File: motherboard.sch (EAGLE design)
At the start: 187 parts, among them IC1 LM2576, IC10 TUSB2046B, IC12 LM50, IC13 LM50, IC2 74LS595D, IC3 74LS595D, IC4 IC_FT230X-SSOP-16, IC5 VN5772AK, IC6 VN5772AK, IC7 VN5772AK, IC8 VN5772AK, IC9 VN5772AK, SW1 FSMSM, U2 NCP4625, U3 ATMEGA168, Y1 16Mhz, Y2 6MHz

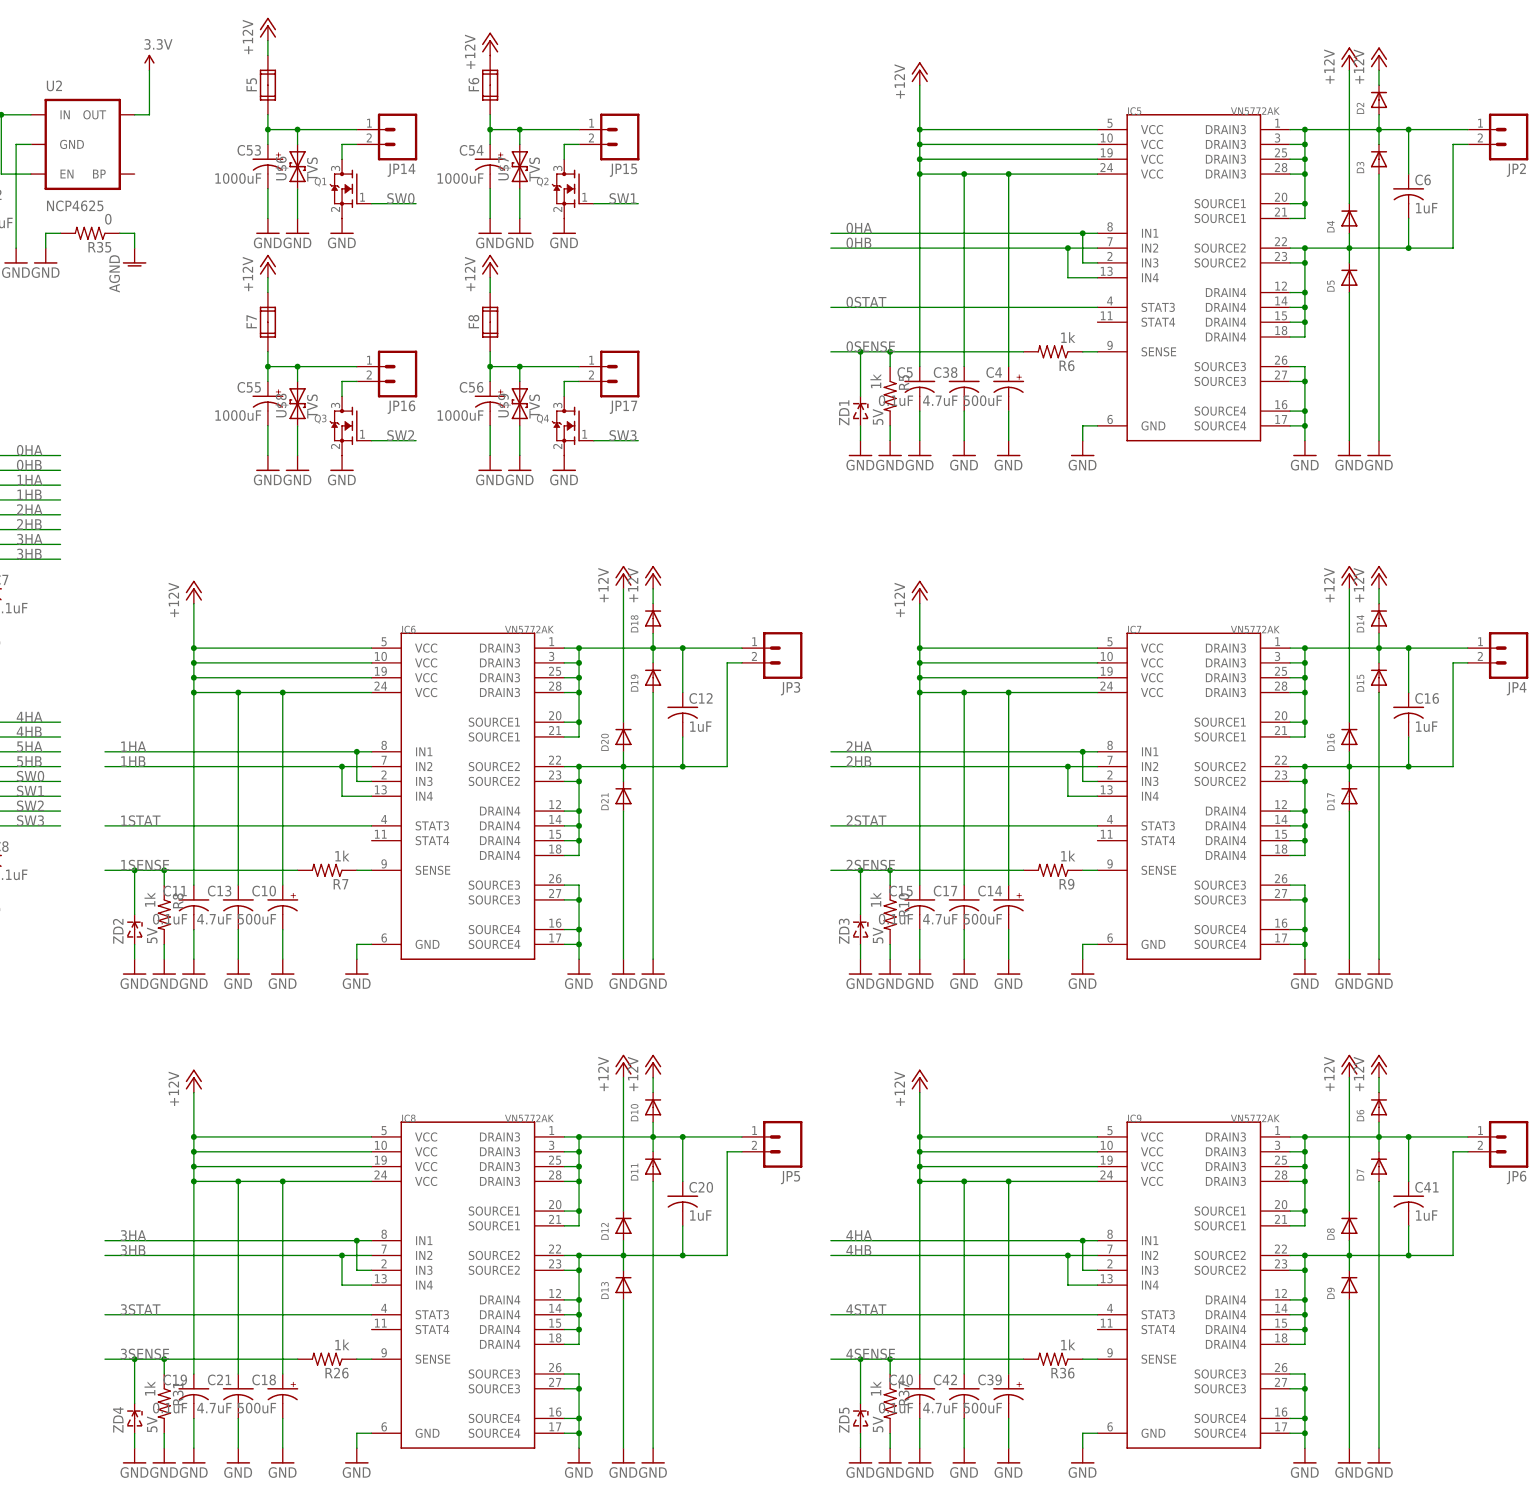
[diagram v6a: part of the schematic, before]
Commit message: rewired h-bridges to not short out and simplified trace layout
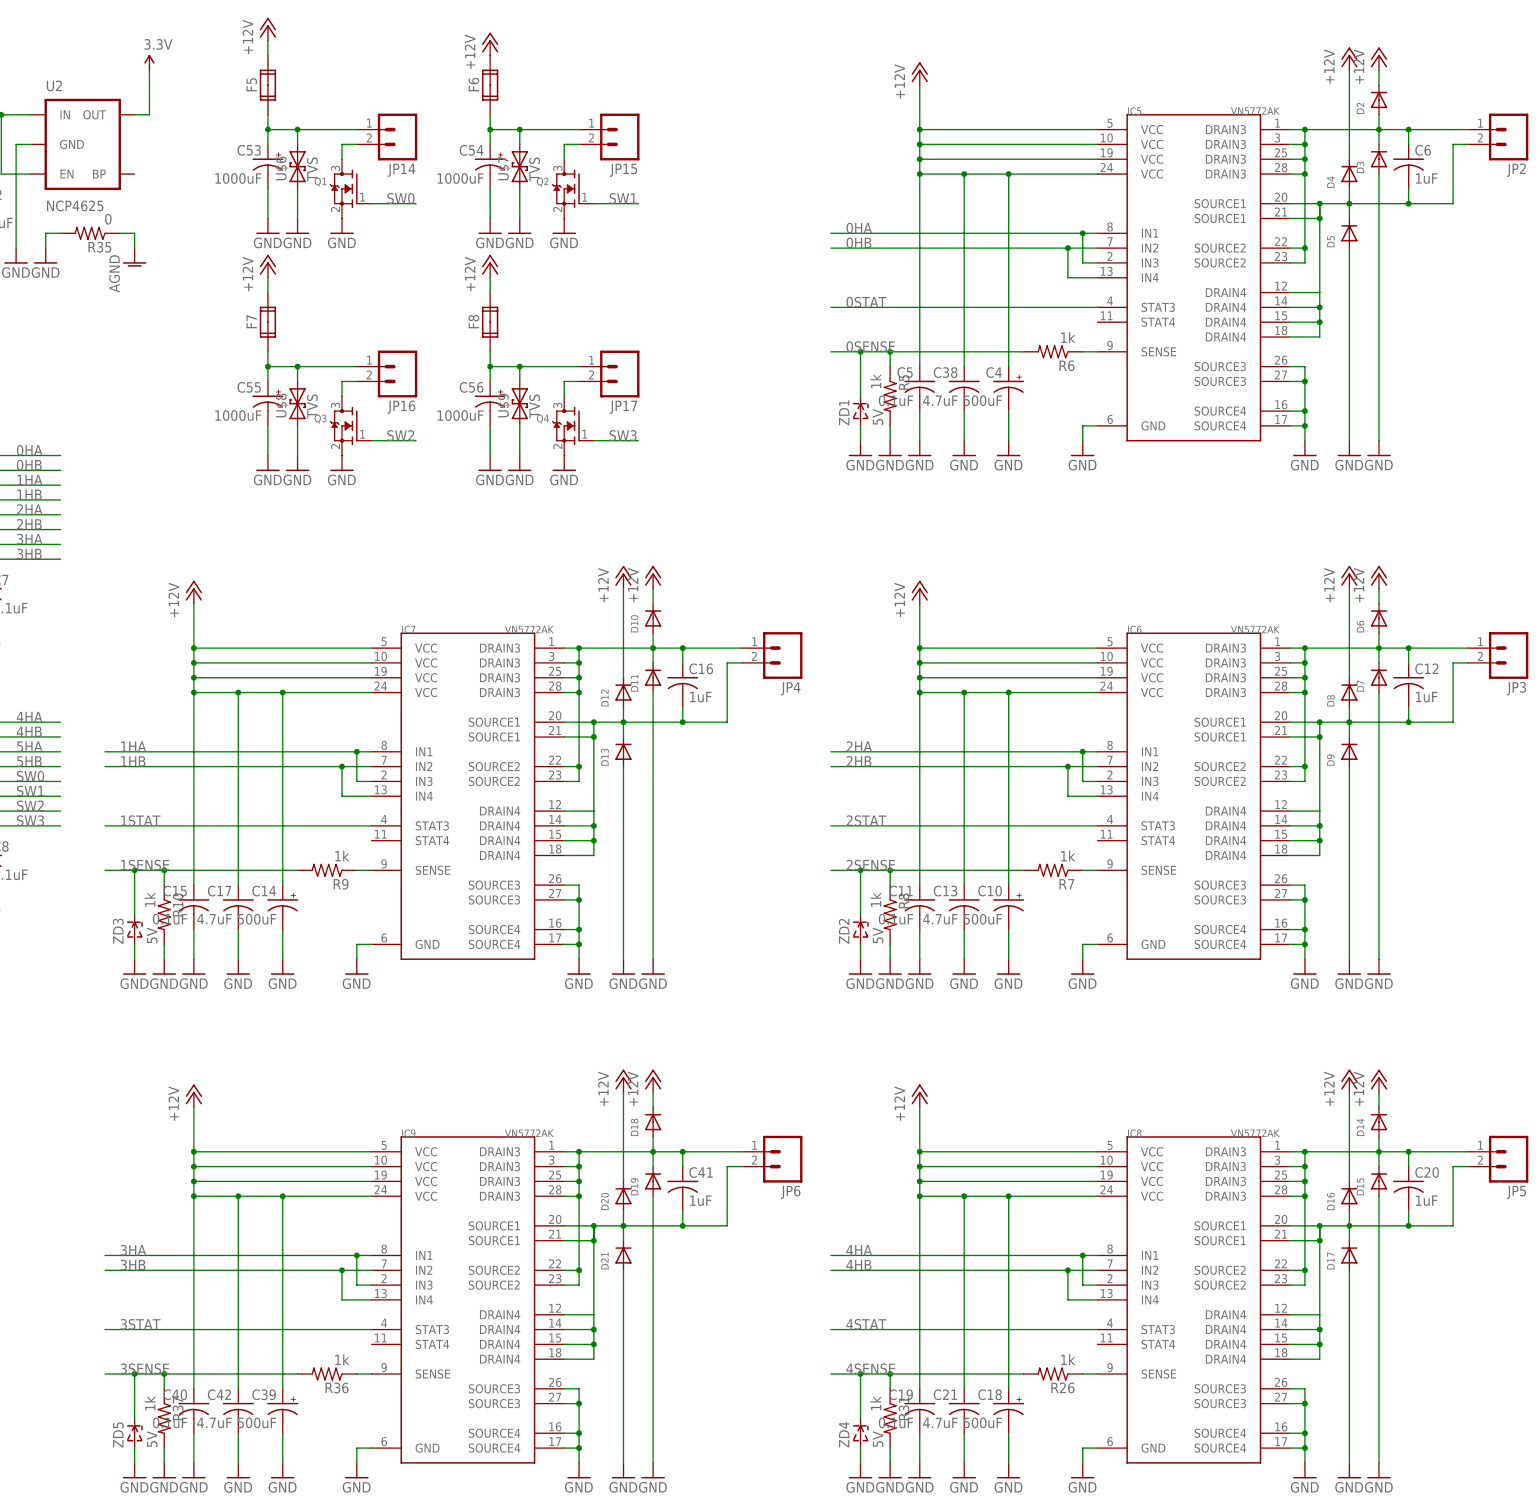
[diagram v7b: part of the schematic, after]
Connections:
- removed net N$15: C41.2, D8.A, D9.C, IC9.DRAIN4@0, IC9.DRAIN4@1, IC9.DRAIN4@2, IC9.DRAIN4@3, IC9.SOURCE2@0, IC9.SOURCE2@1, JP6.2
- new net N$59: C6.1, D2.A, D3.C, IC5.DRAIN3@0, IC5.DRAIN3@1, IC5.DRAIN3@2, IC5.DRAIN3@3, IC5.SOURCE2@0, IC5.SOURCE2@1, JP2.1
- net 1HA: now also IC7.IN1, IC7.IN3; no longer IC6.IN1, IC6.IN3
- net 1HB: now also IC7.IN2, IC7.IN4; no longer IC6.IN2, IC6.IN4
- net 1SENSE: now also R10.1, R9.2, ZD3.C; no longer R7.2, R8.1, ZD2.C
- net 1STAT: now also IC7.STAT3; no longer IC6.STAT3
- net 2HA: now also IC6.IN1, IC6.IN3; no longer IC7.IN1, IC7.IN3
- net 2HB: now also IC6.IN2, IC6.IN4; no longer IC7.IN2, IC7.IN4
- net 2SENSE: now also R7.2, R8.1, ZD2.C; no longer R10.1, R9.2, ZD3.C
- net 2STAT: now also IC6.STAT3; no longer IC7.STAT3
- net 3HA: now also IC9.IN1, IC9.IN3; no longer IC8.IN1, IC8.IN3
- net 3HB: now also IC9.IN2, IC9.IN4; no longer IC8.IN2, IC8.IN4
- net 3SENSE: now also R36.2, R37.1, ZD5.C; no longer R26.2, R31.1, ZD4.C
- net 3STAT: now also IC9.STAT3; no longer IC8.STAT3
- net 4HA: now also IC8.IN1, IC8.IN3; no longer IC9.IN1, IC9.IN3
- net 4HB: now also IC8.IN2, IC8.IN4; no longer IC9.IN2, IC9.IN4
- net 4SENSE: now also R26.2, R31.1, ZD4.C; no longer R36.2, R37.1, ZD5.C
- net 4STAT: now also IC8.STAT3; no longer IC9.STAT3
- net N$10: now also C20.2, D16.A, D17.C, IC8.DRAIN4@0, IC8.DRAIN4@1, IC8.DRAIN4@2, IC8.DRAIN4@3, JP5.2; no longer C20.1, D10.A, D11.C, IC8.DRAIN3@0, IC8.DRAIN3@1, IC8.DRAIN3@2, IC8.DRAIN3@3, JP5.1
- net N$11: now also C20.1, D14.A, D15.C, IC8.DRAIN3@0, IC8.DRAIN3@1, IC8.DRAIN3@2, IC8.DRAIN3@3, IC8.SOURCE2@0, IC8.SOURCE2@1, JP5.1; no longer C6.1, D2.A, D3.C, IC5.DRAIN3@0, IC5.DRAIN3@1, IC5.DRAIN3@2, IC5.DRAIN3@3, IC5.SOURCE1@0, IC5.SOURCE1@1, JP2.1
- net N$12: now also C41.2, D20.A, D21.C, IC9.DRAIN4@0, IC9.DRAIN4@1, IC9.DRAIN4@2, IC9.DRAIN4@3, IC9.SOURCE1@0, IC9.SOURCE1@1, JP6.2; no longer C20.2, D12.A, D13.C, IC8.DRAIN4@0, IC8.DRAIN4@1, IC8.DRAIN4@2, IC8.DRAIN4@3, IC8.SOURCE2@0, IC8.SOURCE2@1, JP5.2
- net N$13: now also IC5.SOURCE1@0, IC5.SOURCE1@1; no longer IC5.SOURCE2@0, IC5.SOURCE2@1
- net N$14: now also D18.A, D19.C, IC9.SOURCE2@0, IC9.SOURCE2@1; no longer D6.A, D7.C, IC9.SOURCE1@0, IC9.SOURCE1@1
- net N$3: now also C12.2, D8.A, D9.C, IC6.DRAIN4@0, IC6.DRAIN4@1, IC6.DRAIN4@2, IC6.DRAIN4@3, JP3.2; no longer C12.1, D18.A, D19.C, IC6.DRAIN3@0, IC6.DRAIN3@1, IC6.DRAIN3@2, IC6.DRAIN3@3, JP3.1
- net N$5: now also C12.1, D6.A, D7.C, IC6.DRAIN3@0, IC6.DRAIN3@1, IC6.DRAIN3@2, IC6.DRAIN3@3, JP3.1; no longer C12.2, D20.A, D21.C, IC6.DRAIN4@0, IC6.DRAIN4@1, IC6.DRAIN4@2, IC6.DRAIN4@3, JP3.2
- net N$8: now also C16.2, D12.A, D13.C, IC7.DRAIN4@0, IC7.DRAIN4@1, IC7.DRAIN4@2, IC7.DRAIN4@3, JP4.2; no longer C16.1, D14.A, D15.C, IC7.DRAIN3@0, IC7.DRAIN3@1, IC7.DRAIN3@2, IC7.DRAIN3@3, JP4.1
- net N$9: now also C16.1, D10.A, D11.C, IC7.DRAIN3@0, IC7.DRAIN3@1, IC7.DRAIN3@2, IC7.DRAIN3@3, JP4.1; no longer C16.2, D16.A, D17.C, IC7.DRAIN4@0, IC7.DRAIN4@1, IC7.DRAIN4@2, IC7.DRAIN4@3, JP4.2
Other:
- moved on the sheet: C10, C11, C12, C13, C14, C15, C16, C17, C18, C19, C20, C21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

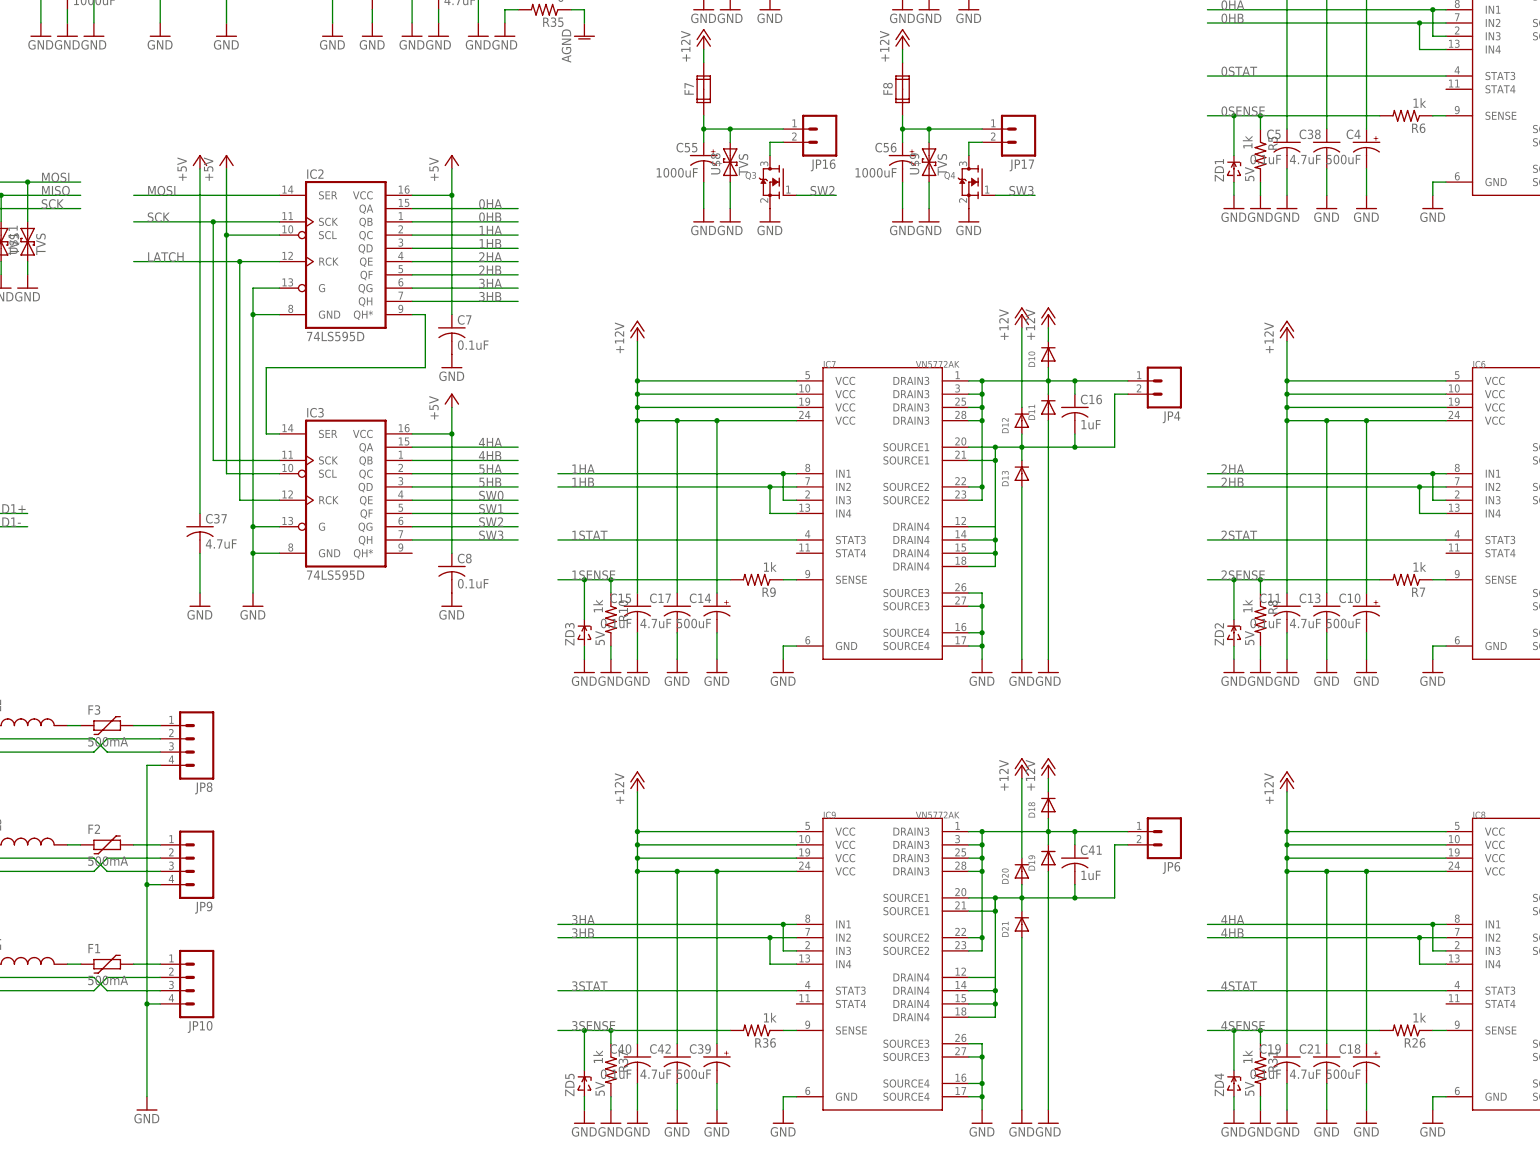
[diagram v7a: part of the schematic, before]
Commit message: added current liminting resistors to shift registers
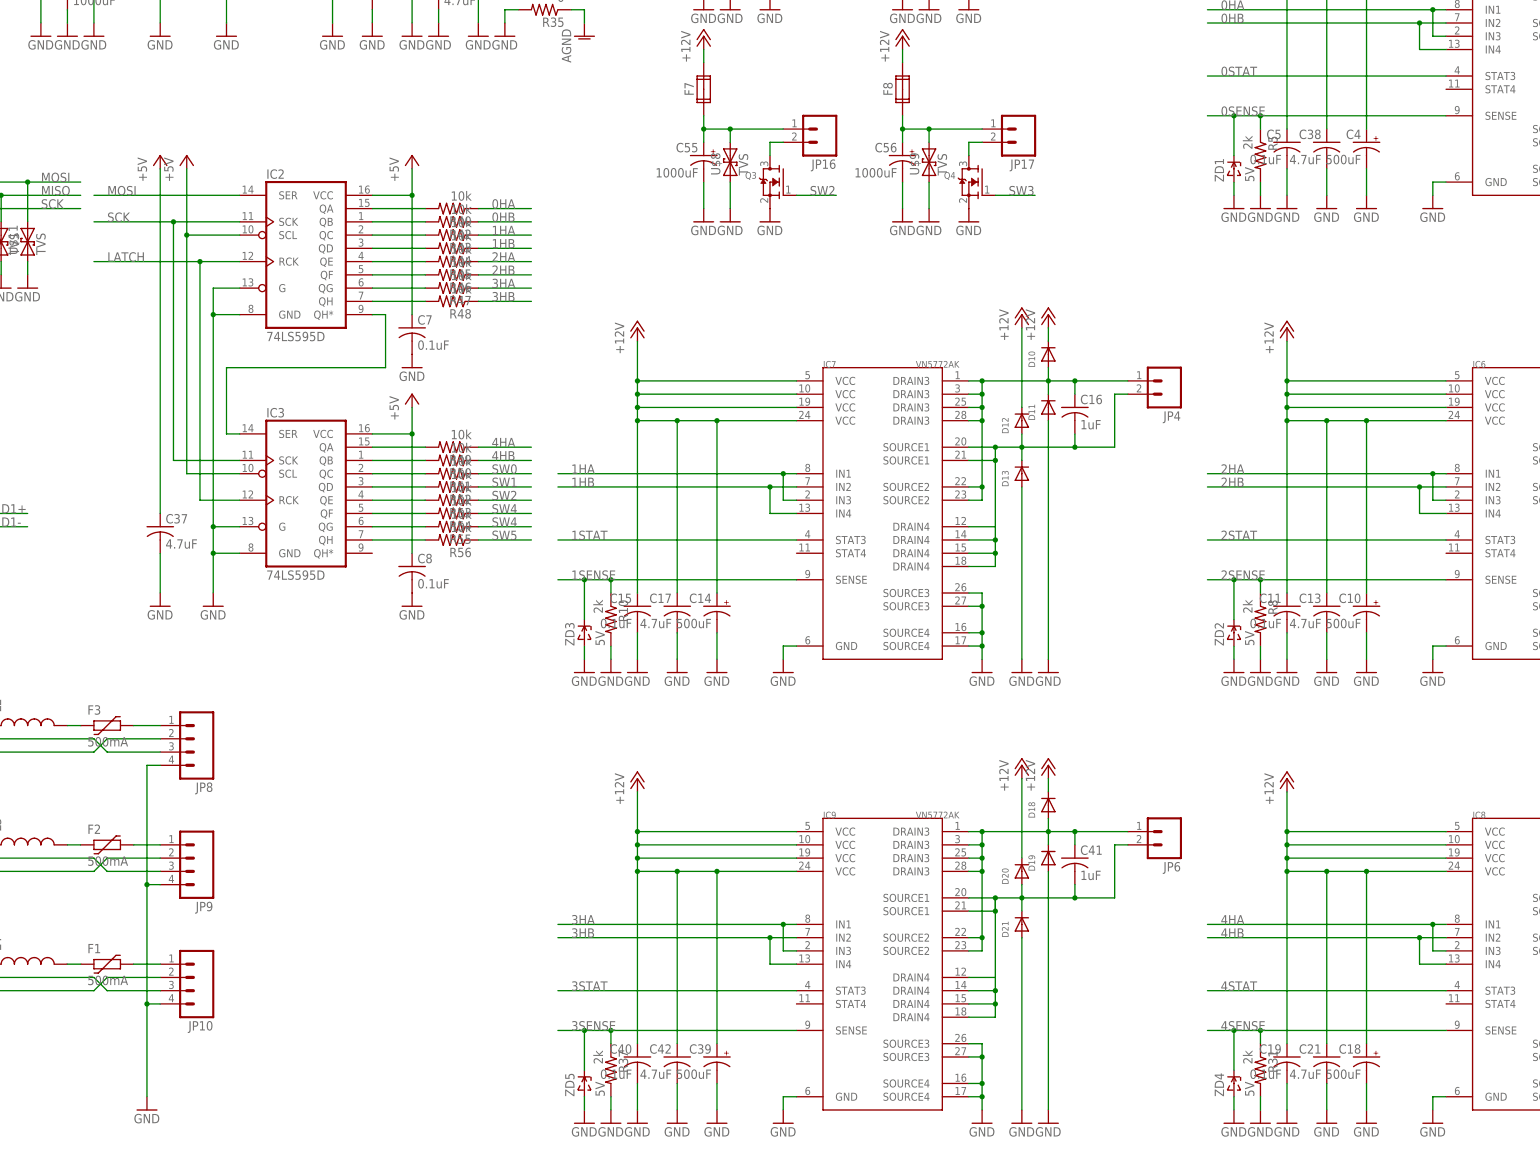
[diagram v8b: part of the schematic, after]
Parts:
- removed R26, R36, R6, R7, R9: 1k, adafruit:R-US_R1206
- added R40, R42, R43, R44, R45, R46, R47, R48, R49, R50, R51, R52, R53, R54, R55, R56: 10k, adafruit:R-US_R1206
- R10, R31, R37, R5, R8: value 1k -> 2k
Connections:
- removed net 5HA: IC3.QC
- removed net 5HB: IC3.QD
- new net N$15: IC3.QH, R56.2
- new net N$17: IC3.QG, R55.2
- new net N$18: IC3.QF, R54.2
- new net N$56: IC3.QE, R53.2
- new net N$60: IC3.QD, R52.2
- new net N$61: IC3.QC, R51.2
- new net N$62: IC3.QB, R50.2
- new net N$63: IC3.QA, R49.2
- new net N$64: IC2.QH, R48.2
- new net N$65: IC2.QG, R47.2
- new net N$66: IC2.QF, R46.2
- new net N$67: IC2.QE, R45.2
- new net N$68: IC2.QD, R44.2
- new net N$69: IC2.QC, R43.2
- new net N$70: IC2.QB, R42.2
- new net N$71: IC2.QA, R40.2
- new net SW4: R54.1, R55.1
- new net SW5: R56.1
- net 0HA: now also R40.1; no longer IC2.QA
- net 0HB: now also R42.1; no longer IC2.QB
- net 0SENSE: no longer IC6.SENSE, IC7.SENSE, IC8.SENSE, IC9.SENSE, R26.1, R36.1, R6.1, R6.2, R7.1, R9.1
- net 1HA: now also R43.1; no longer IC2.QC
- net 1HB: now also R44.1; no longer IC2.QD
- net 1SENSE: now also IC7.SENSE; no longer R9.2
- net 2HA: now also R45.1; no longer IC2.QE
- net 2HB: now also R46.1; no longer IC2.QF
- net 2SENSE: now also IC6.SENSE; no longer R7.2
- net 3HA: now also R47.1; no longer IC2.QG
- net 3HB: now also R48.1; no longer IC2.QH
- net 3SENSE: now also IC9.SENSE; no longer R36.2
- net 4HA: now also R49.1; no longer IC3.QA
- net 4HB: now also R50.1; no longer IC3.QB
- net 4SENSE: now also IC8.SENSE; no longer R26.2
- net SW0: now also R51.1; no longer IC3.QE
- net SW1: now also R52.1; no longer IC3.QF
- net SW2: now also R53.1; no longer IC3.QG
- net SW3: no longer IC3.QH
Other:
- moved on the sheet: C37, C7, C8, IC2, IC3
